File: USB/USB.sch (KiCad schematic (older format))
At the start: 30 parts

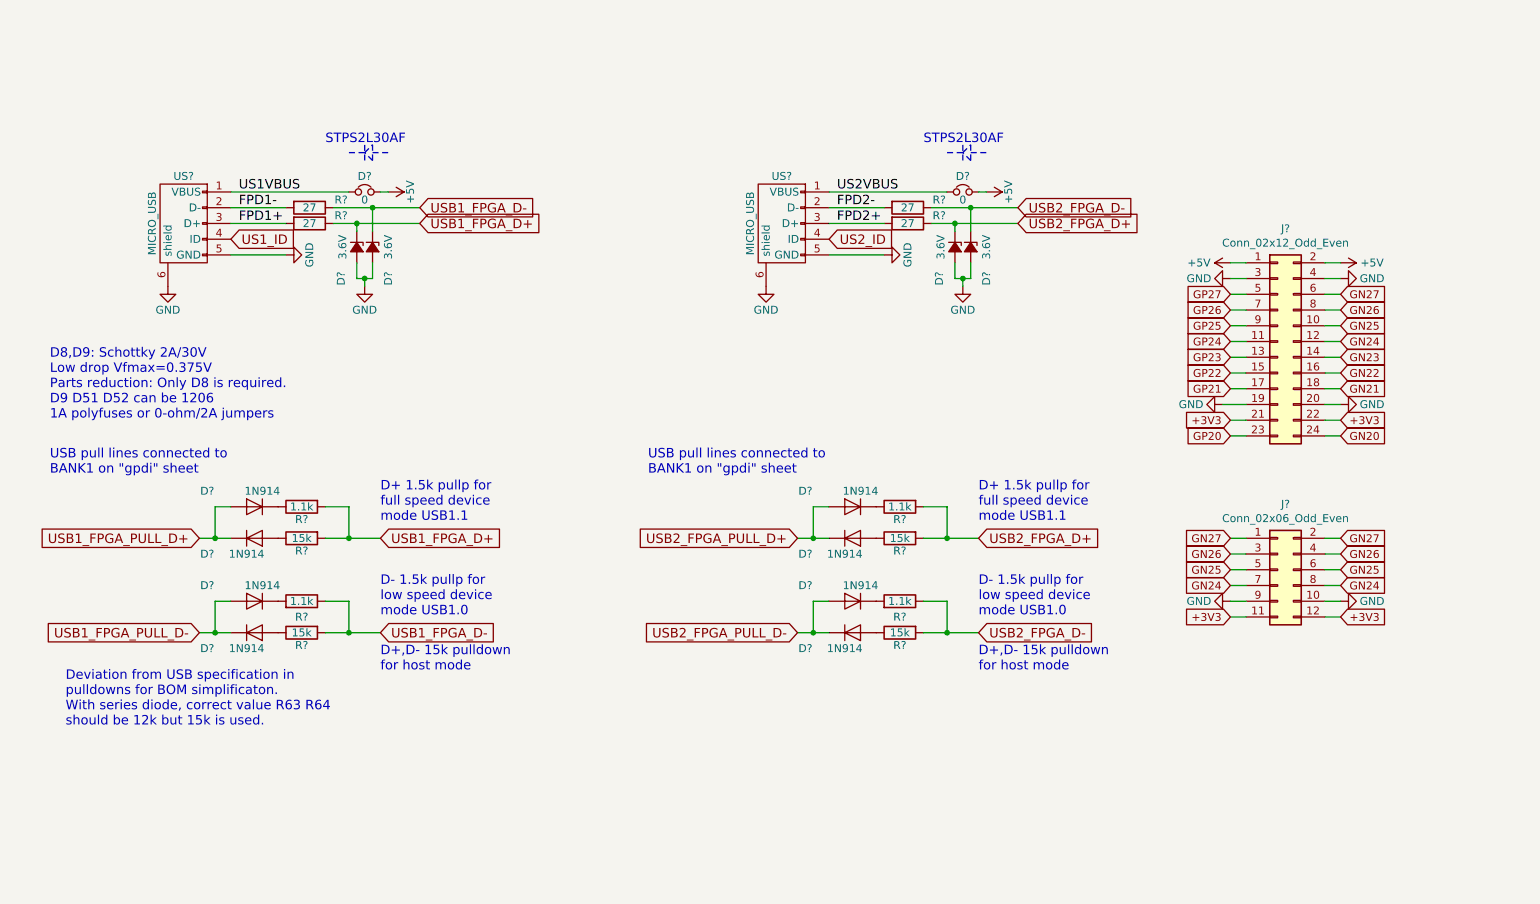
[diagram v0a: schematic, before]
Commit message: all routed with micro USB connectors
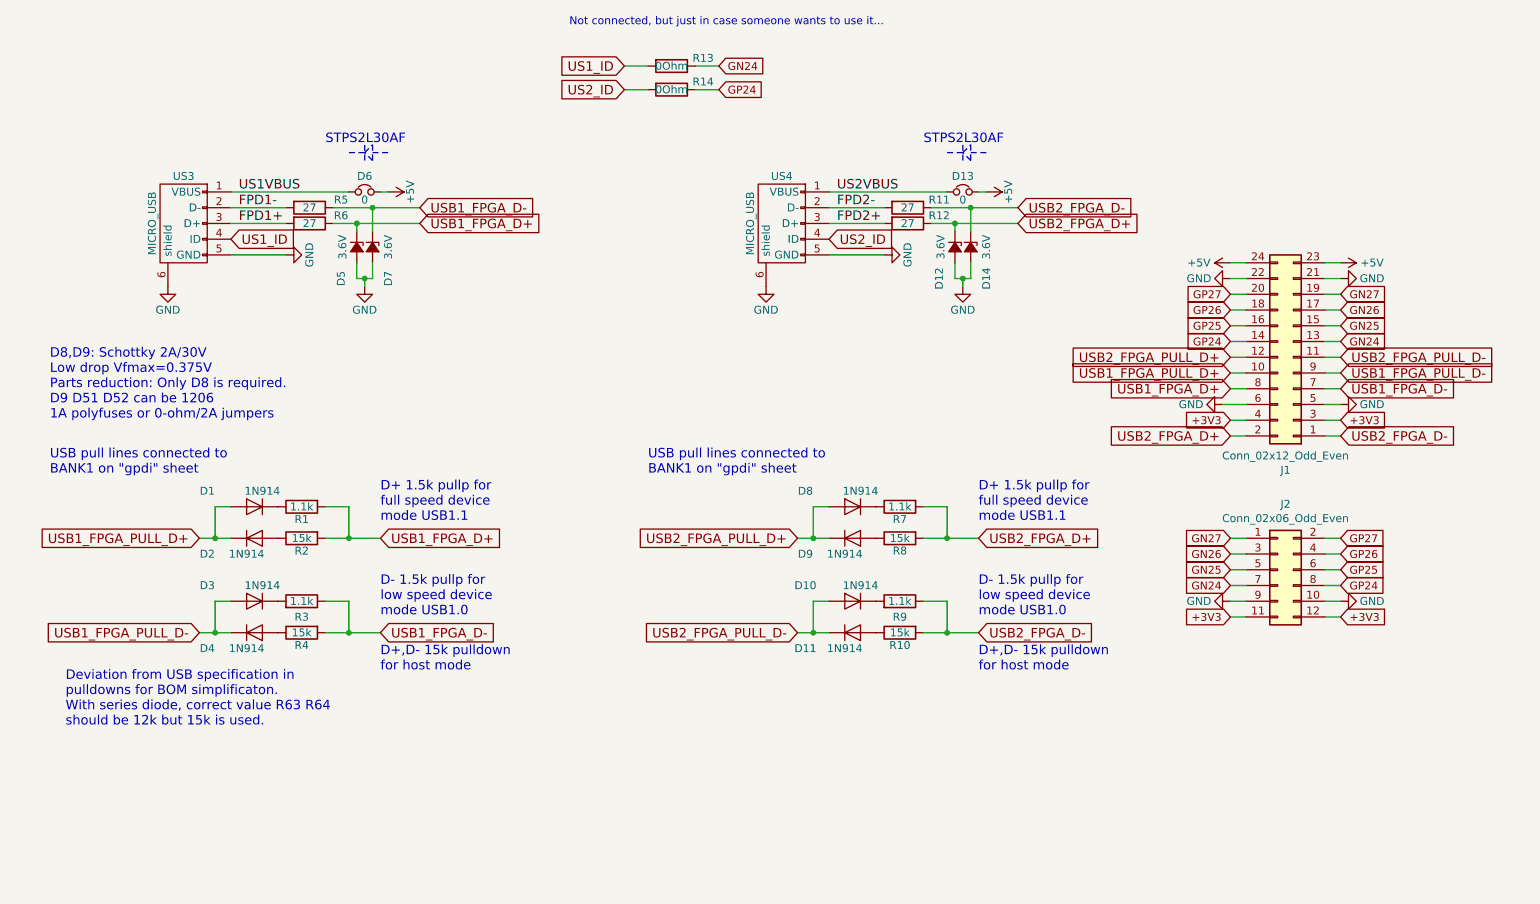
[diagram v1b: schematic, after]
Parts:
- added R13, R14: 0Ohm, Resistor_SMD:R_0603_1608Metric, symbol Device:R
- J1: renamed from J?; footprint (none) -> Connector_PinHeader_2.54mm:PinHeader_2x12_P2.54mm_Horizontal
- J2: renamed from J?; footprint (none) -> Connector_PinHeader_2.54mm:PinHeader_2x06_P2.54mm_Horizontal
- gave numbers to parts that had none: 28
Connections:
- net GN20 is gone; now on net +5V: J1.24 (Pin_24)
- net GN21 is gone; now on net GP26: J1.18 (Pin_18)
- net GN22 is gone; now on net GP25: J1.16 (Pin_16)
- net GN23 is gone; now on net GP24: J1.14 (Pin_14)
- net GP20 is gone; now on net +5V: J1.23 (Pin_23)
- net GP21 is gone; now on net GN26: J1.17 (Pin_17)
- net GP22 is gone; now on net GN25: J1.15 (Pin_15)
- net GP23 is gone; now on net GN24: J1.13 (Pin_13)
- net +3V3: now also J1.3 (Pin_3), J1.4 (Pin_4); no longer J1.21 (Pin_21), J1.22 (Pin_22)
- net +5V: no longer J1.1 (Pin_1), J1.2 (Pin_2)
- net GN24: now also R13.1; no longer J1.12 (Pin_12), J2.8 (Pin_8)
- net GN25: no longer J1.10 (Pin_10), J2.6 (Pin_6)
- net GN26: no longer J1.8 (Pin_8), J2.4 (Pin_4)
- net GN27: now also J1.19 (Pin_19); no longer J1.6 (Pin_6), J2.2 (Pin_2)
- net GND: now also J1.21 (Pin_21), J1.22 (Pin_22), J1.5 (Pin_5), J1.6 (Pin_6); no longer J1.19 (Pin_19), J1.20 (Pin_20), J1.3 (Pin_3), J1.4 (Pin_4)
- net GP24: now also J2.8 (Pin_8), R14.1; no longer J1.11 (Pin_11)
- net GP25: now also J2.6 (Pin_6); no longer J1.9 (Pin_9)
- net GP26: now also J2.4 (Pin_4); no longer J1.7 (Pin_7)
- net GP27: now also J1.20 (Pin_20), J2.2 (Pin_2); no longer J1.5 (Pin_5)
- net US1_ID: now also R13.2
- net US2_ID: now also R14.2
- net USB1_FPGA_D+: now also J1.8 (Pin_8)
- net USB1_FPGA_D-: now also J1.7 (Pin_7)
- net USB1_FPGA_PULL_D+: now also J1.10 (Pin_10)
- net USB1_FPGA_PULL_D-: now also J1.9 (Pin_9)
- net USB2_FPGA_D+: now also J1.2 (Pin_2)
- net USB2_FPGA_D-: now also J1.1 (Pin_1)
- net USB2_FPGA_PULL_D+: now also J1.12 (Pin_12)
- net USB2_FPGA_PULL_D-: now also J1.11 (Pin_11)
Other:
- note added: "Not connected, but just in case someone wants to use it..."

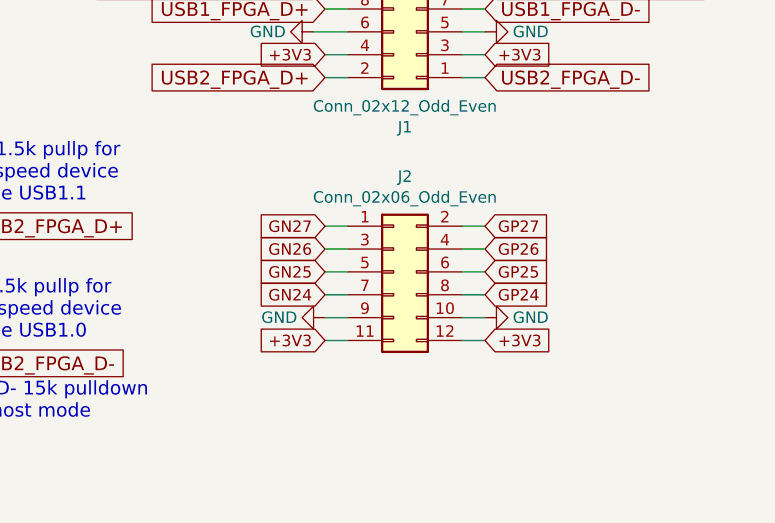
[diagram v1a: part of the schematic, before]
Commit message: Adding female connector for PMOD
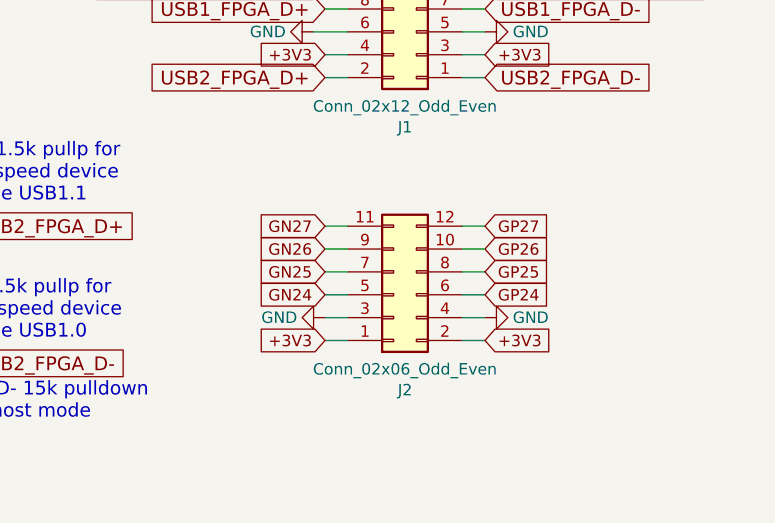
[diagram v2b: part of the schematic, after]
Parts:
- J2: footprint Connector_PinHeader_2.54mm:PinHeader_2x06_P2.54mm_Horizontal -> Connector_PinSocket_2.54mm:PinSocket_2x06_P2.54mm_Horizontal
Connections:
- net +3V3: now also J2.1 (Pin_1), J2.2 (Pin_2); no longer J2.11 (Pin_11), J2.12 (Pin_12)
- net GN24: now also J2.5 (Pin_5); no longer J2.7 (Pin_7)
- net GN25: now also J2.7 (Pin_7); no longer J2.5 (Pin_5)
- net GN26: now also J2.9 (Pin_9); no longer J2.3 (Pin_3)
- net GN27: now also J2.11 (Pin_11); no longer J2.1 (Pin_1)
- net GND: now also J2.3 (Pin_3), J2.4 (Pin_4); no longer J2.10 (Pin_10), J2.9 (Pin_9)
- net GP24: now also J2.6 (Pin_6); no longer J2.8 (Pin_8)
- net GP25: now also J2.8 (Pin_8); no longer J2.6 (Pin_6)
- net GP26: now also J2.10 (Pin_10); no longer J2.4 (Pin_4)
- net GP27: now also J2.12 (Pin_12); no longer J2.2 (Pin_2)
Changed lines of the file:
@@
 L Connector_Generic:Conn_02x06_Odd_Even J2
 U 1 1 5DFAA8B3
-P 9350 4400
-F 0 "J2" H 9400 4817 50  0000 C CNN
-F 1 "Conn_02x06_Odd_Even" H 9400 4726 50  0000 C CNN
-F 2 "Connector_PinHeader_2.54mm:PinHeader_2x06_P2.54mm_Horizontal" H 9350 4400 50  0001 C CNN
-F 3 "~" H 9350 4400 50  0001 C CNN
-	1    9350 4400
-	1    0    0    -1
+P 9350 4500
+F 0 "J2" H 9400 4917 50  0000 C CNN
+F 1 "Conn_02x06_Odd_Even" H 9400 4826 50  0000 C CNN
+F 2 "Connector_PinSocket_2.54mm:PinSocket_2x06_P2.54mm_Horizontal" H 9350 4500 50  0001 C CNN
+F 3 "~" H 9350 4500 50  0001 C CNN
+	1    9350 4500
+	1    0    0    1
 $EndComp
 $EndSCHEMATC

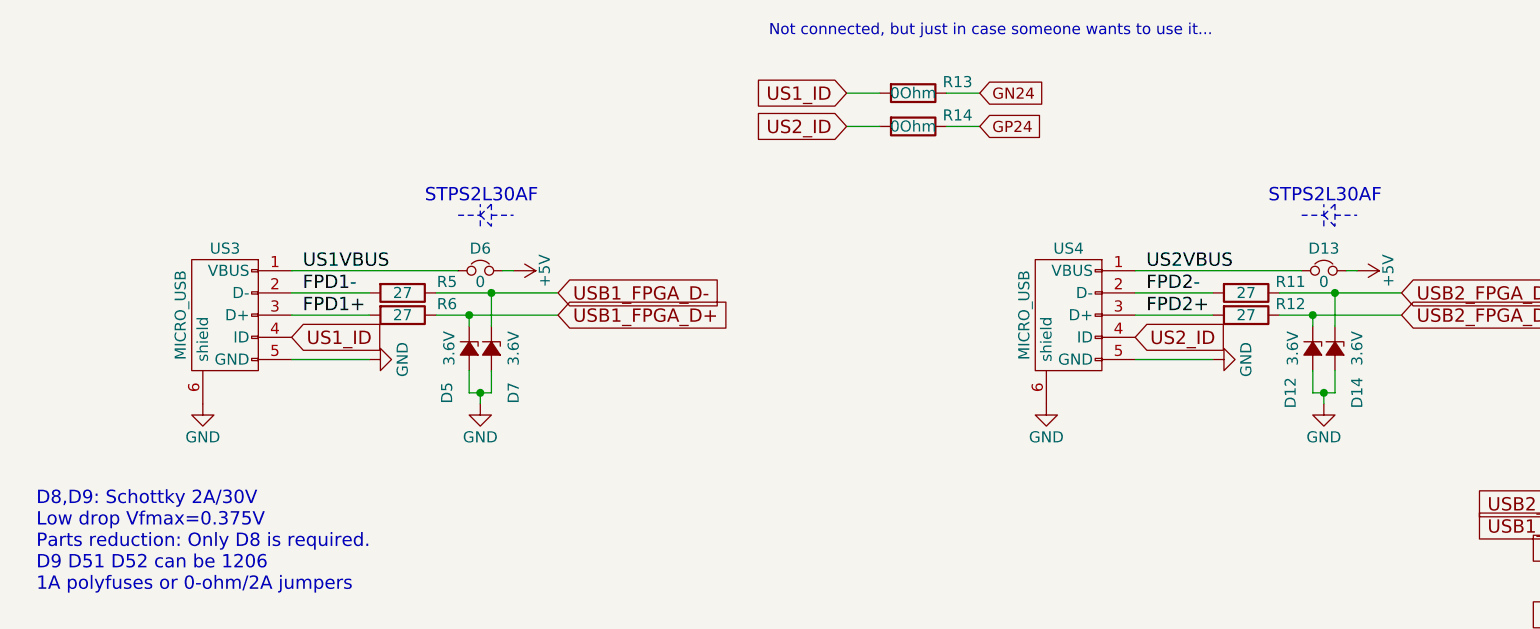
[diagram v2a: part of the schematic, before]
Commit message: Adding USB-A 3D model
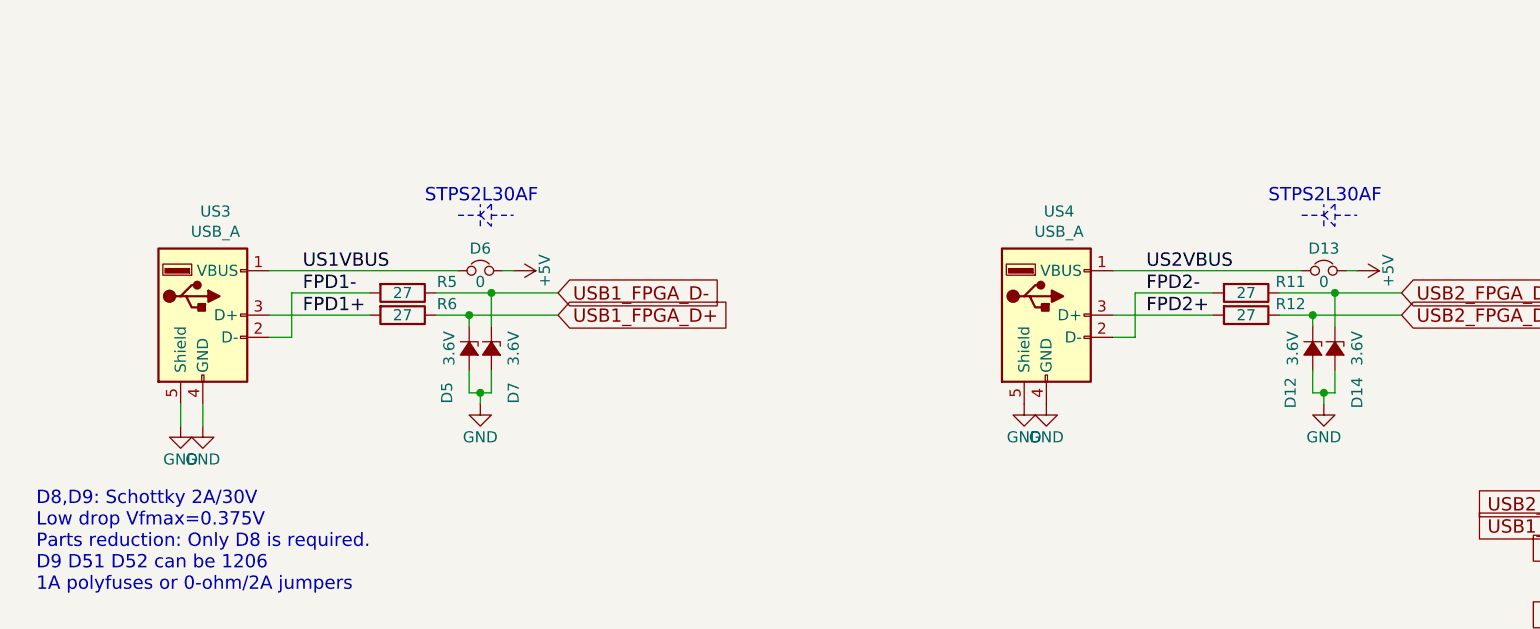
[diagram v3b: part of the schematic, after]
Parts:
- removed R13, R14: 0Ohm, Resistor_SMD:R_0603_1608Metric, symbol Device:R
- removed US3, US4: MICRO_USB, usb_otg:USB-MICRO-B-FCI-10118192-0001LF, symbol usb_otg:USB_OTG
- added US3, US4: USB_A, Connector_USB:USB_A_Stewart_SS-52100-001_Horizontal, symbol Connector:USB_A
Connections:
- net FPD1+: now also US3.3 (D+)
- net FPD1-: now also US3.2 (D-)
- net FPD2+: now also US4.3 (D+)
- net FPD2-: now also US4.2 (D-)
- net GND: now also US3.4 (GND), US3.5 (Shield), US4.4 (GND), US4.5 (Shield)
- net US1VBUS: now also US3.1 (VBUS)
- net US2VBUS: now also US4.1 (VBUS)
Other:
- note removed: "Not connected, but just in case someone wants to use it..."
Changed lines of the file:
@@
 EESchema Schematic File Version 4
-LIBS:USB-cache
 EELAYER 30 0
 EELAYER END
@@
 	0    1    1    0
 $EndComp
-$Comp
-L usb_otg:USB_OTG US3
-U 1 1 58D6C841
-P 2400 2200
-AR Path="/58D6C841" Ref="US3"  Part="1"
-AR Path="/58D6BF46/58D6C841" Ref="US?"  Part="1"
-F 0 "US3" V 2100 2200 50  0000 C CNN
-F 1 "MICRO_USB" H 2400 2400 50  0000 C CNN
-F 2 "usb_otg:USB-MICRO-B-FCI-10118192-0001LF" V 2350 2100 50  0001 C CNN
-F 3 "portal.fciconnect.com/Comergent/fci/drawing/10118192.pdf" H 2350 2100 50  0001 C CNN
-	1    2400 2200
-	0    -1   1    0
-$EndComp
-$Comp
-L power:GND #PWR02
-U 1 1 58D6C843
-P 3050 2400
-F 0 "#PWR02" H 3050 2150 50  0001 C CNN
-F 1 "GND" H 3050 2250 50  0000 C CNN
-F 2 "" H 3050 2400 50  0000 C CNN
-F 3 "" H 3050 2400 50  0000 C CNN
-	1    3050 2400
-	0    -1   -1   0
-$EndComp
 Text GLabel 3900 2100 2    60   Input ~ 0
 USB1_FPGA_D-
@@
 L power:GND #PWR01
 U 1 1 58D8254A
-P 2300 2600
-F 0 "#PWR01" H 2300 2350 50  0001 C CNN
-F 1 "GND" H 2300 2450 50  0000 C CNN
-F 2 "" H 2300 2600 50  0000 C CNN
-F 3 "" H 2300 2600 50  0000 C CNN
-	1    2300 2600
+P 2300 2700
+F 0 "#PWR01" H 2300 2450 50  0001 C CNN
+F 1 "GND" H 2300 2550 50  0000 C CNN
+F 2 "" H 2300 2700 50  0000 C CNN
+F 3 "" H 2300 2700 50  0000 C CNN
+	1    2300 2700
 	1    0    0    -1
 $EndComp
@@
 	3650 2000 3700 2000
 Wire Wire Line
-	2700 2000 3450 2000
-Wire Wire Line
-	2700 2400 3050 2400
-Wire Wire Line
 	2700 2100 3050 2100
-Wire Wire Line
-	2700 2200 3050 2200
 $Comp
 L Device:R R1
@@
 Text Notes 3300 1700 0    60   ~ 0
 STPS2L30AF
-Text GLabel 2700 2300 2    60   Input ~ 0
-US1_ID
 $Comp
 L Device:Jumper_NC_Small D13
@@
 	0    1    1    0
 $EndComp
-$Comp
-L usb_otg:USB_OTG US4
-U 1 1 5DF4B6ED
-P 6200 2200
-AR Path="/5DF4B6ED" Ref="US4"  Part="1"
-AR Path="/58D6BF46/5DF4B6ED" Ref="US?"  Part="1"
-F 0 "US4" V 5900 2200 50  0000 C CNN
-F 1 "MICRO_USB" H 6200 2400 50  0000 C CNN
-F 2 "usb_otg:USB-MICRO-B-FCI-10118192-0001LF" V 6150 2100 50  0001 C CNN
-F 3 "portal.fciconnect.com/Comergent/fci/drawing/10118192.pdf" H 6150 2100 50  0001 C CNN
-	1    6200 2200
-	0    -1   1    0
-$EndComp
-$Comp
-L power:GND #PWR06
-U 1 1 5DF4B6F7
-P 6850 2400
-F 0 "#PWR06" H 6850 2150 50  0001 C CNN
-F 1 "GND" H 6850 2250 50  0000 C CNN
-F 2 "" H 6850 2400 50  0000 C CNN
-F 3 "" H 6850 2400 50  0000 C CNN
-	1    6850 2400
-	0    -1   -1   0
-$EndComp
 Text GLabel 7700 2100 2    60   Input ~ 0
 USB2_FPGA_D-
@@
 	7450 2000 7500 2000
 Wire Wire Line
-	6500 2000 7250 2000
-Wire Wire Line
-	6500 2400 6850 2400
-Wire Wire Line
 	6500 2100 6850 2100
-Wire Wire Line
-	6500 2200 6850 2200
 $Comp
 L Device:R R7
@@
 Text Notes 7100 1700 0    60   ~ 0
 STPS2L30AF
-Text GLabel 6500 2300 2    60   Input ~ 0
-US2_ID
 $Bitmap
 Pos 9400 1400
@@
 USB2_FPGA_PULL_D-
 $Comp
-L Device:R R13
-U 1 1 5DF38F4F
-P 5500 1200
-AR Path="/5DF38F4F" Ref="R13"  Part="1"
-AR Path="/58D6BF46/5DF38F4F" Ref="R?"  Part="1"
-F 0 "R13" V 5450 1400 50  0000 C CNN
-F 1 "0Ohm" V 5500 1200 50  0000 C CNN
-F 2 "Resistor_SMD:R_0603_1608Metric" V 5430 1200 50  0001 C CNN
-F 3 "" H 5500 1200 50  0000 C CNN
-F 4 "www.yageo.com" V 5500 1200 50  0001 C CNN "MNF1_URL"
-F 5 "AC0603JR-0727RL" V 5500 1200 50  0001 C CNN "MPN"
-	1    5500 1200
-	0    1    1    0
-$EndComp
-$Comp
-L Device:R R14
-U 1 1 5DF395CD
-P 5500 1350
-AR Path="/5DF395CD" Ref="R14"  Part="1"
-AR Path="/58D6BF46/5DF395CD" Ref="R?"  Part="1"
-F 0 "R14" V 5450 1550 50  0000 C CNN
-F 1 "0Ohm" V 5500 1350 50  0000 C CNN
-F 2 "Resistor_SMD:R_0603_1608Metric" V 5430 1350 50  0001 C CNN
-F 3 "" H 5500 1350 50  0000 C CNN
-F 4 "www.yageo.com" V 5500 1350 50  0001 C CNN "MNF1_URL"
-F 5 "AC0603JR-0727RL" V 5500 1350 50  0001 C CNN "MPN"
-	1    5500 1350
-	0    1    1    0
-$EndComp
-Text GLabel 5200 1200 0    60   Input ~ 0
-US1_ID
-Text GLabel 5200 1350 0    60   Input ~ 0
-US2_ID
-Text GLabel 5800 1350 2    50   Input ~ 0
-GP24
-Text GLabel 5800 1200 2    50   Input ~ 0
-GN24
-Wire Wire Line
-	5200 1200 5350 1200
-Wire Wire Line
-	5650 1200 5800 1200
-Wire Wire Line
-	5200 1350 5350 1350
-Wire Wire Line
-	5650 1350 5800 1350
-Text Notes 4850 950  0    50   ~ 0
-Not connected, but just in case someone wants to use it...
-$Comp
 L Connector_Generic:Conn_02x06_Odd_Even J2
 U 1 1 5DFAA8B3
@@
 	1    0    0    1
 $EndComp
+$Comp
+L Connector:USB_A US4
+U 1 1 5DF9BA2D
+P 6100 2200
+F 0 "US4" H 6157 2667 50  0000 C CNN
+F 1 "USB_A" H 6157 2576 50  0000 C CNN
+F 2 "Connector_USB:USB_A_Stewart_SS-52100-001_Horizontal" H 6250 2150 50  0001 C CNN
+F 3 " ~" H 6250 2150 50  0001 C CNN
+	1    6100 2200
+	1    0    0    -1
+$EndComp
+$Comp
+L Connector:USB_A US3
+U 1 1 5DF9C01F
+P 2300 2200
+F 0 "US3" H 2357 2667 50  0000 C CNN
+F 1 "USB_A" H 2357 2576 50  0000 C CNN
+F 2 "Connector_USB:USB_A_Stewart_SS-52100-001_Horizontal" H 2450 2150 50  0001 C CNN
+F 3 " ~" H 2450 2150 50  0001 C CNN
+	1    2300 2200
+	1    0    0    -1
+$EndComp
+$Comp
+L power:GND #PWR0101
+U 1 1 5DF9EB7F
+P 6000 2600
+F 0 "#PWR0101" H 6000 2350 50  0001 C CNN
+F 1 "GND" H 6000 2450 50  0000 C CNN
+F 2 "" H 6000 2600 50  0000 C CNN
+F 3 "" H 6000 2600 50  0000 C CNN
+	1    6000 2600
+	1    0    0    -1
+$EndComp
+Wire Wire Line
+	6400 2200 6850 2200
+Wire Wire Line
+	6400 2300 6500 2300
+Wire Wire Line
+	6500 2300 6500 2100
+Wire Wire Line
+	6400 2000 7250 2000
+Wire Wire Line
+	2300 2700 2300 2600
+$Comp
+L power:GND #PWR0102
+U 1 1 5DFB033D
+P 2200 2700
+F 0 "#PWR0102" H 2200 2450 50  0001 C CNN
+F 1 "GND" H 2200 2550 50  0000 C CNN
+F 2 "" H 2200 2700 50  0000 C CNN
+F 3 "" H 2200 2700 50  0000 C CNN
+	1    2200 2700
+	1    0    0    -1
+$EndComp
+Wire Wire Line
+	2200 2600 2200 2700
+Wire Wire Line
+	2600 2200 3050 2200
+Wire Wire Line
+	2600 2300 2700 2300
+Wire Wire Line
+	2700 2300 2700 2100
+Wire Wire Line
+	2600 2000 3450 2000
 $EndSCHEMATC
